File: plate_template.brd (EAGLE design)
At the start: 80 x 44 mm, 32 parts, among them J1 CON-10SWD, J2 CON-10SWD, J3 USB-5PIN10118193, J4 CON-2CON-HEADER-2, J5 CON-2CON-HEADER-2, J8 CON-26

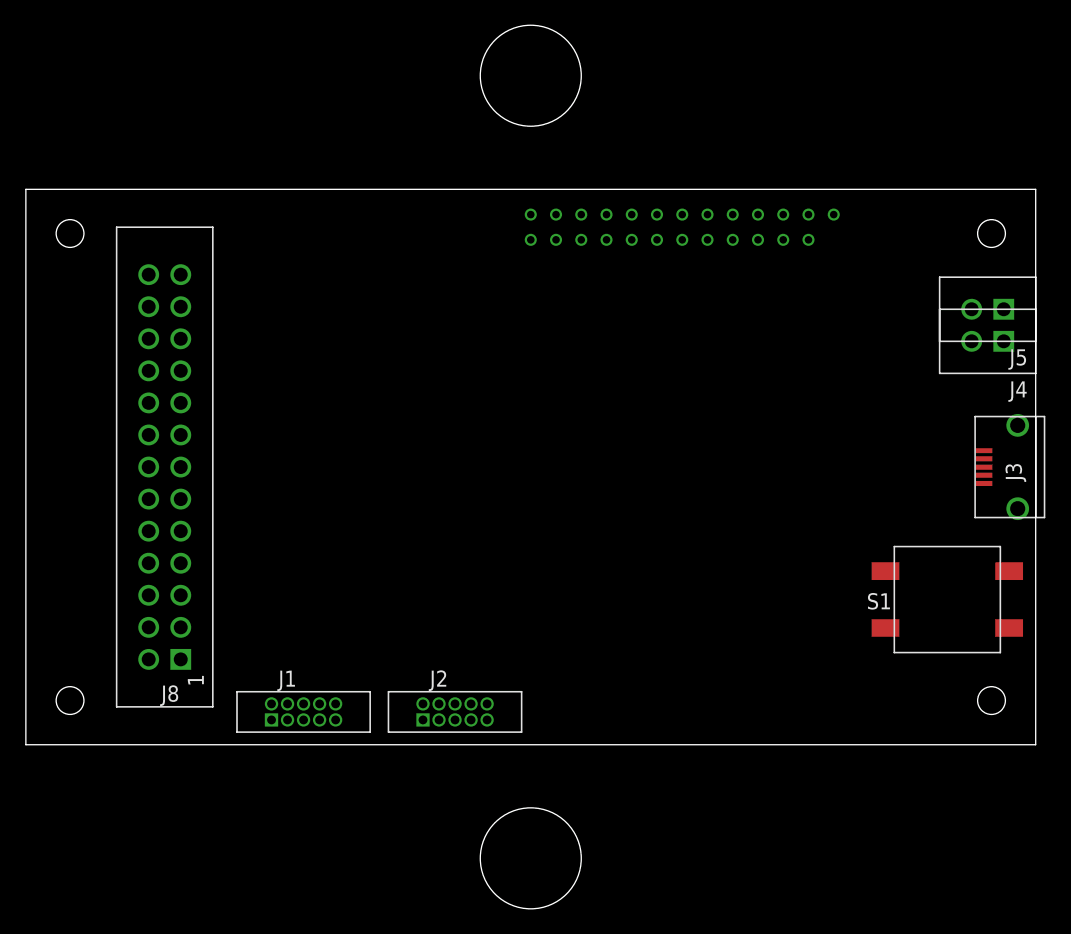
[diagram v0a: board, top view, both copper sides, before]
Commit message: add cutout for header pins
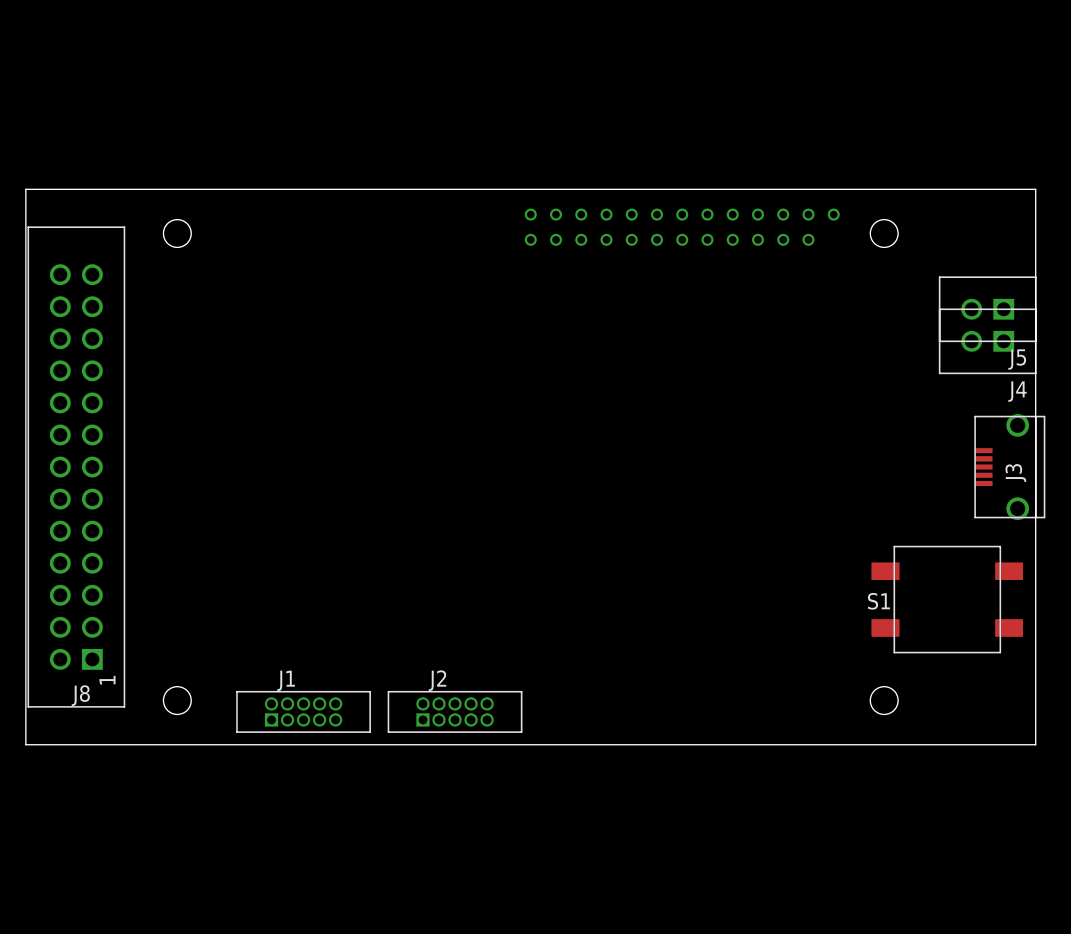
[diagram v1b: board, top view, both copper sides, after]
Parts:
- moved J8 7.00 mm to (-36.0, 0.00)
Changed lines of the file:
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@@
 <wire x1="40" y1="22" x2="40" y2="-22" width="0.1" layer="20"/>
 <wire x1="40" y1="-22" x2="-40" y2="-22" width="0.1" layer="20"/>
-<hole x="-36.5" y="18.5" drill="2.2"/>
-<hole x="-36.5" y="-18.5" drill="2.2"/>
-<hole x="36.5" y="18.5" drill="2.2"/>
-<hole x="36.5" y="-18.5" drill="2.2"/>
-<hole x="0" y="-31" drill="8"/>
-<hole x="0" y="31" drill="8"/>
-<wire x1="-50" y1="-40" x2="50" y2="-40" width="0.4064" layer="49"/>
-<wire x1="50" y1="-40" x2="50" y2="40" width="0.4064" layer="49"/>
-<wire x1="50" y1="40" x2="-50" y2="40" width="0.4064" layer="49"/>
-<wire x1="-50" y1="40" x2="-50" y2="-40" width="0.4064" layer="49"/>
+<hole x="-28" y="18.5" drill="2.2"/>
+<hole x="-28" y="-18.5" drill="2.2"/>
+<hole x="28" y="18.5" drill="2.2"/>
+<hole x="28" y="-18.5" drill="2.2"/>
 </plain>
 <attributes>
@@
 <attribute name="POGO_DIAMETER" value="1.8" x="24" y="20" size="1.778" layer="27" display="off"/>
 </element>
-<element name="J8" library="firefly" package="CON-HEADER-2X13" value="CON-26" x="-29" y="0" rot="R90">
-<attribute name="ORDERING-CODE" value="68602-126HLF" x="-29" y="0" size="1.778" layer="27" rot="R90" display="off"/>
-<attribute name="MANUFACTURER" value="Amphenol FCI" x="-29" y="0" size="1.778" layer="27" rot="R90" display="off"/>
+<element name="J8" library="firefly" package="CON-HEADER-2X13" value="CON-26" x="-36" y="0" rot="R90">
+<attribute name="ORDERING-CODE" value="68602-126HLF" x="-36" y="0" size="1.778" layer="27" rot="R90" display="off"/>
+<attribute name="MANUFACTURER" value="Amphenol FCI" x="-36" y="0" size="1.778" layer="27" rot="R90" display="off"/>
 </element>
 <element name="J3" library="firefly" package="10118193" value="USB-5PIN10118193" x="35.9" y="0" rot="R90">
@@
 <contactref element="J8" pad="4"/>
 <contactref element="J3" pad="5"/>
-<wire x1="-30.27" y1="12.7" x2="-30.27" y2="-12.7" width="0" layer="19" extent="1-1"/>
-<wire x1="-27.73" y1="12.7" x2="-30.27" y2="12.7" width="0" layer="19" extent="1-1"/>
-<wire x1="-27.73" y1="15.24" x2="-27.73" y2="12.7" width="0" layer="19" extent="1-1"/>
-<wire x1="-3.46" y1="-20.035" x2="-27.73" y2="15.24" width="0" layer="19" extent="1-1"/>
+<wire x1="-37.27" y1="12.7" x2="-37.27" y2="-12.7" width="0" layer="19" extent="1-1"/>
+<wire x1="-34.73" y1="12.7" x2="-37.27" y2="12.7" width="0" layer="19" extent="1-1"/>
+<wire x1="-34.73" y1="15.24" x2="-34.73" y2="12.7" width="0" layer="19" extent="1-1"/>
+<wire x1="-3.46" y1="-20.035" x2="-34.73" y2="15.24" width="0" layer="19" extent="1-1"/>
 <wire x1="-6" y1="-20.035" x2="-3.46" y2="-20.035" width="0" layer="19" extent="1-1"/>
 <wire x1="-7.27" y1="-20.035" x2="-6" y2="-20.035" width="0" layer="19" extent="1-1"/>
@@
 <contactref element="J3" pad="1"/>
 <wire x1="18" y1="20" x2="35.9" y2="-1.3" width="0" layer="19" extent="1-1"/>
-<wire x1="-30.27" y1="0" x2="35.9" y2="-1.3" width="0" layer="19" extent="1-1"/>
+<wire x1="-37.27" y1="0" x2="35.9" y2="-1.3" width="0" layer="19" extent="1-1"/>
 </signal>
 <signal name="DUT_USB_D+">
@@
 <contactref element="TP_USB_D-" pad="1"/>
 <contactref element="J3" pad="2"/>
-<wire x1="35.9" y1="-0.65" x2="-30.27" y2="-2.54" width="0" layer="19" extent="1-1"/>
+<wire x1="35.9" y1="-0.65" x2="-37.27" y2="-2.54" width="0" layer="19" extent="1-1"/>
 <wire x1="16" y1="18" x2="35.9" y2="-0.65" width="0" layer="19" extent="1-1"/>
 </signal>
@@
 <contactref element="J3" pad="3"/>
 <wire x1="18" y1="18" x2="35.9" y2="0" width="0" layer="19" extent="1-1"/>
-<wire x1="-27.73" y1="0" x2="35.9" y2="0" width="0" layer="19" extent="1-1"/>
+<wire x1="-34.73" y1="0" x2="35.9" y2="0" width="0" layer="19" extent="1-1"/>
 </signal>
 <signal name="DUT_BUTTON+">
@@
 <contactref element="TP_BUTTON" pad="1"/>
 <wire x1="4" y1="18" x2="37.9" y2="-8.25" width="0" layer="19" extent="1-1"/>
-<wire x1="-27.73" y1="-2.54" x2="4" y2="18" width="0" layer="19" extent="1-1"/>
+<wire x1="-34.73" y1="-2.54" x2="4" y2="18" width="0" layer="19" extent="1-1"/>
 <contactref element="S1" pad="B2"/>
 </signal>
@@
 <contactref element="TP_BATTERY+" pad="1"/>
 <wire x1="12" y1="18" x2="37.47" y2="9.96" width="0" layer="19" extent="1-1"/>
-<wire x1="-30.27" y1="2.54" x2="37.47" y2="9.96" width="0" layer="19" extent="1-1"/>
+<wire x1="-37.27" y1="2.54" x2="37.47" y2="9.96" width="0" layer="19" extent="1-1"/>
 </signal>
 <signal name="DUT_MOTOR+">
@@
 <contactref element="J5" pad="1"/>
 <wire x1="37.47" y1="12.5" x2="6" y2="18" width="0" layer="19" extent="1-1"/>
-<wire x1="-30.27" y1="15.24" x2="37.47" y2="12.5" width="0" layer="19" extent="1-1"/>
+<wire x1="-37.27" y1="15.24" x2="37.47" y2="12.5" width="0" layer="19" extent="1-1"/>
 </signal>
 <signal name="DUT_MCU1_NRESET">
@@
 <contactref element="J1" pad="10"/>
 <contactref element="TP_NRF_NRESET" pad="1"/>
-<wire x1="-15.46" y1="-18.765" x2="-27.73" y2="-10.16" width="0" layer="19" extent="1-1"/>
+<wire x1="-15.46" y1="-18.765" x2="-34.73" y2="-10.16" width="0" layer="19" extent="1-1"/>
 <wire x1="0" y1="18" x2="-15.46" y2="-18.765" width="0" layer="19" extent="1-1"/>
 </signal>
@@
 <contactref element="J1" pad="4"/>
 <contactref element="TP_NRF_SWDCLK" pad="1"/>
-<wire x1="-19.27" y1="-18.765" x2="-27.73" y2="-12.7" width="0" layer="19" extent="1-1"/>
+<wire x1="-19.27" y1="-18.765" x2="-34.73" y2="-12.7" width="0" layer="19" extent="1-1"/>
 <wire x1="2" y1="18" x2="-19.27" y2="-18.765" width="0" layer="19" extent="1-1"/>
 </signal>
@@
 <contactref element="J1" pad="2"/>
 <contactref element="TP_NRF_DIO" pad="1"/>
-<wire x1="-20.54" y1="-18.765" x2="-30.27" y2="-15.24" width="0" layer="19" extent="1-1"/>
+<wire x1="-20.54" y1="-18.765" x2="-37.27" y2="-15.24" width="0" layer="19" extent="1-1"/>
 <wire x1="2" y1="20" x2="-20.54" y2="-18.765" width="0" layer="19" extent="1-1"/>
 </signal>
@@
 <contactref element="J1" pad="1"/>
 <contactref element="TP_VCC" pad="1"/>
-<wire x1="-20.54" y1="-20.035" x2="-27.73" y2="-15.24" width="0" layer="19" extent="1-1"/>
+<wire x1="-20.54" y1="-20.035" x2="-34.73" y2="-15.24" width="0" layer="19" extent="1-1"/>
 <wire x1="0" y1="20" x2="-20.54" y2="-20.035" width="0" layer="19" extent="1-1"/>
 </signal>
@@
 <contactref element="J2" pad="10"/>
 <contactref element="TP_STM_NRESET" pad="1"/>
-<wire x1="-3.46" y1="-18.765" x2="-27.73" y2="-5.08" width="0" layer="19" extent="1-1"/>
+<wire x1="-3.46" y1="-18.765" x2="-34.73" y2="-5.08" width="0" layer="19" extent="1-1"/>
 <wire x1="22" y1="20" x2="-3.46" y2="-18.765" width="0" layer="19" extent="1-1"/>
 </signal>
@@
 <contactref element="J2" pad="4"/>
 <contactref element="TP_STM_SWDCLK" pad="1"/>
-<wire x1="-7.27" y1="-18.765" x2="-27.73" y2="-7.62" width="0" layer="19" extent="1-1"/>
+<wire x1="-7.27" y1="-18.765" x2="-34.73" y2="-7.62" width="0" layer="19" extent="1-1"/>
 <wire x1="20" y1="20" x2="-7.27" y2="-18.765" width="0" layer="19" extent="1-1"/>
 </signal>
@@
 <contactref element="J2" pad="2"/>
 <contactref element="TP_STM_SWDIO" pad="1"/>
-<wire x1="-8.54" y1="-18.765" x2="-30.27" y2="-10.16" width="0" layer="19" extent="1-1"/>
+<wire x1="-8.54" y1="-18.765" x2="-37.27" y2="-10.16" width="0" layer="19" extent="1-1"/>
 <wire x1="20" y1="18" x2="-8.54" y2="-18.765" width="0" layer="19" extent="1-1"/>
 </signal>
@@
 <contactref element="J2" pad="1"/>
 <contactref element="TP_VAUX2" pad="1"/>
-<wire x1="-8.54" y1="-20.035" x2="-30.27" y2="-7.62" width="0" layer="19" extent="1-1"/>
+<wire x1="-8.54" y1="-20.035" x2="-37.27" y2="-7.62" width="0" layer="19" extent="1-1"/>
 <wire x1="22" y1="18" x2="-8.54" y2="-20.035" width="0" layer="19" extent="1-1"/>
 </signal>
@@
 <contactref element="J8" pad="10"/>
 <contactref element="TP_BOOT0" pad="1"/>
-<wire x1="16" y1="20" x2="-30.27" y2="-5.08" width="0" layer="19" extent="1-1"/>
+<wire x1="16" y1="20" x2="-37.27" y2="-5.08" width="0" layer="19" extent="1-1"/>
 </signal>
 <signal name="DUT_I2C_DRDY">
 <contactref element="J8" pad="18"/>
 <contactref element="TP_SEN_DRDY" pad="1"/>
-<wire x1="8" y1="20" x2="-30.27" y2="5.08" width="0" layer="19" extent="1-1"/>
+<wire x1="8" y1="20" x2="-37.27" y2="5.08" width="0" layer="19" extent="1-1"/>
 </signal>
 <signal name="DUT_I2C_SDA">
 <contactref element="J8" pad="17"/>
 <contactref element="TP_SEN_SDA" pad="1"/>
-<wire x1="8" y1="18" x2="-27.73" y2="5.08" width="0" layer="19" extent="1-1"/>
+<wire x1="8" y1="18" x2="-34.73" y2="5.08" width="0" layer="19" extent="1-1"/>
 </signal>
 <signal name="DUT_I2C_SCL">
 <contactref element="J8" pad="20"/>
 <contactref element="TP_SEN_SCL" pad="1"/>
-<wire x1="-30.27" y1="7.62" x2="10" y2="20" width="0" layer="19" extent="1-1"/>
+<wire x1="-37.27" y1="7.62" x2="10" y2="20" width="0" layer="19" extent="1-1"/>
 </signal>
 <signal name="DUT_SPI_MOSI">
 <contactref element="J8" pad="21"/>
 <contactref element="TP_SPI_MOSI" pad="1"/>
-<wire x1="14" y1="20" x2="-27.73" y2="10.16" width="0" layer="19" extent="1-1"/>
+<wire x1="14" y1="20" x2="-34.73" y2="10.16" width="0" layer="19" extent="1-1"/>
 </signal>
 <signal name="DUT_SPI_MISO">
 <contactref element="J8" pad="22"/>
 <contactref element="TP_SPI_MISO" pad="1"/>
-<wire x1="-30.27" y1="10.16" x2="6" y2="20" width="0" layer="19" extent="1-1"/>
+<wire x1="-37.27" y1="10.16" x2="6" y2="20" width="0" layer="19" extent="1-1"/>
 </signal>
 <signal name="DUT_SPI_SCLK">
 <contactref element="J8" pad="19"/>
 <contactref element="TP_SCLK" pad="1"/>
-<wire x1="14" y1="18" x2="-27.73" y2="7.62" width="0" layer="19" extent="1-1"/>
+<wire x1="14" y1="18" x2="-34.73" y2="7.62" width="0" layer="19" extent="1-1"/>
 </signal>
 <signal name="DUT_VB">

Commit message: plate updates
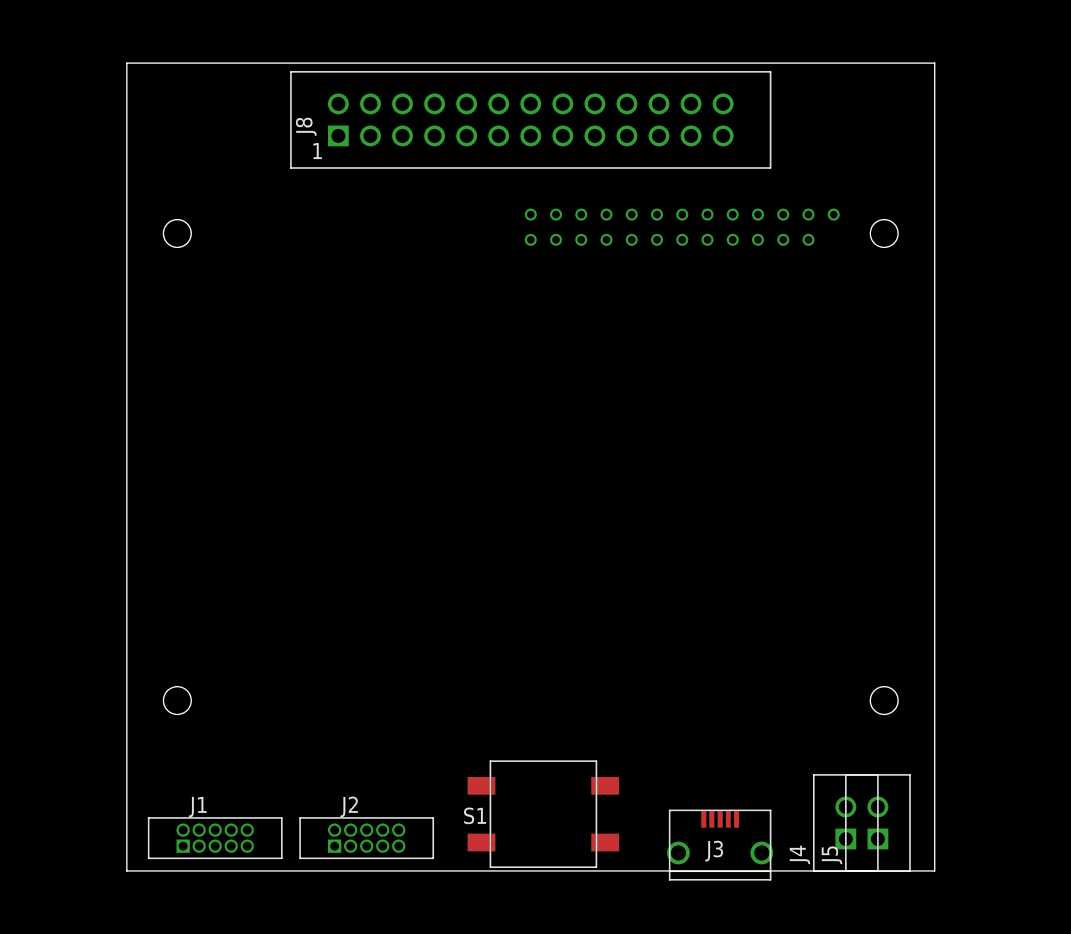
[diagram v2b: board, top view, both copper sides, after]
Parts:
- moved J8 45.3 mm to (0.00, 27.5), turned to 0 degrees
- moved J5 41.6 mm to (27.5, -28.2), turned to 0 degrees
- moved J4 39.8 mm to (25.0, -28.2), turned to 0 degrees
- moved S1 36.2 mm to (1.00, -27.5)
- moved J3 34.9 mm to (15.0, -27.9), turned to 0 degrees
- moved J1 12.2 mm to (-25.0, -29.4)
- moved J2 12.2 mm to (-13.0, -29.4)
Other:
- board size 80 x 44 mm -> 64 x 64 mm
